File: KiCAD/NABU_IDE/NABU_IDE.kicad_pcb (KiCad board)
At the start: 2 copper layers, 80.8 x 69.5 mm, 18 parts, among them J1 IDE ATA Bus, J2 NABU Expansion Header, U1 74LS245, U2 74LS32, U3 74LS08, U4 74LS04, U5 74LS32, U6 74LS574, U7 74LS574

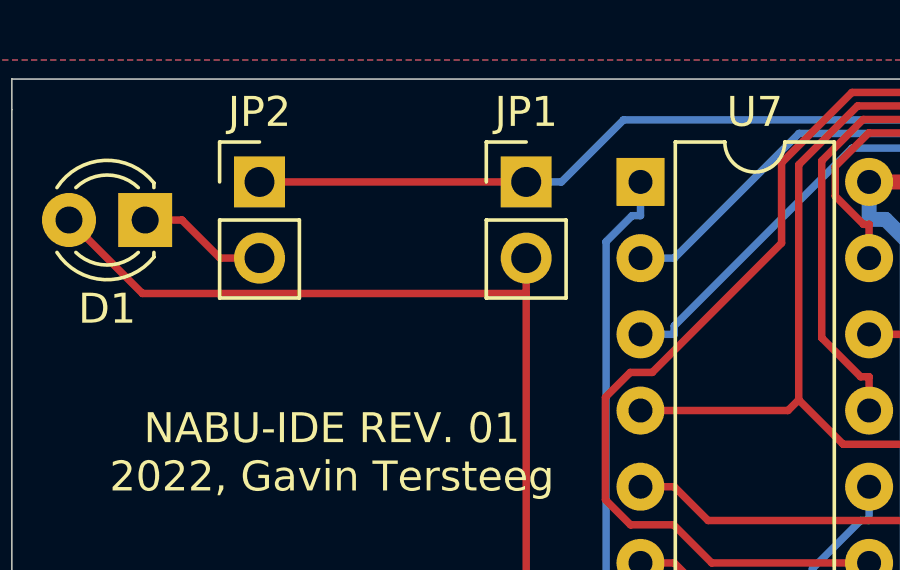
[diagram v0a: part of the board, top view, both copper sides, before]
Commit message: Changed schematics to allow for daisy chaining
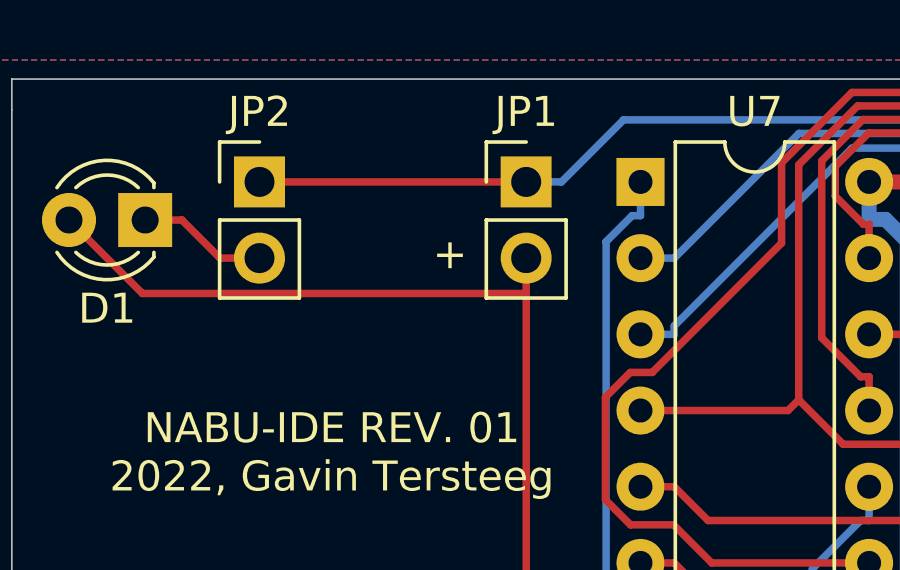
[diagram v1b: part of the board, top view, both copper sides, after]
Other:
- board text added: "+"
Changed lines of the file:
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@@
   (general
     (thickness 1.6)
-    (drawings 8)
+    (drawings 9)
     (tracks 862)
     (zones 0)
@@
     )
   )
+  (gr_text "+\n" (at 193.04 81.788) (layer F.SilkS)
+    (effects (font (size 1 1) (thickness 0.15)))
+  )
   (gr_line (start 259.207 141.097) (end 259.207 145.415) (layer Edge.Cuts) (width 0.05))

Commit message: Started work on new PCB layout
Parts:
- added C2: 100nf, Capacitor_THT:C_Rect_L7.2mm_W2.5mm_P5.00mm_FKS2_FKP2_MKS2_MKP2, F.Cu at (126.9, 54.1)
- added C3: 100nf, Capacitor_THT:C_Rect_L7.2mm_W2.5mm_P5.00mm_FKS2_FKP2_MKS2_MKP2, F.Cu at (116.0, 70.2)
- added C4: 100nf, Capacitor_THT:C_Rect_L7.2mm_W2.5mm_P5.00mm_FKS2_FKP2_MKS2_MKP2, F.Cu at (94.3, 77.0)
- added C5: 100nf, Capacitor_THT:C_Rect_L7.2mm_W2.5mm_P5.00mm_FKS2_FKP2_MKS2_MKP2, F.Cu at (94.3, 81.1)
- added C6: 100nf, Capacitor_THT:C_Rect_L7.2mm_W2.5mm_P5.00mm_FKS2_FKP2_MKS2_MKP2, F.Cu at (94.3, 85.1)
- added C7: 100nf, Capacitor_THT:C_Rect_L7.2mm_W2.5mm_P5.00mm_FKS2_FKP2_MKS2_MKP2, F.Cu at (83.5, 100.5)
- added C8: 100nf, Capacitor_THT:C_Rect_L7.2mm_W2.5mm_P5.00mm_FKS2_FKP2_MKS2_MKP2, F.Cu at (94.3, 89.2)
- added J3: NABU Daisy Chain In, Connector_PinHeader_2.54mm:PinHeader_1x30_P2.54mm_Vertical, F.Cu at (37.8, 50.3)
- added J4: NABU Daisy Chain Out, Connector_PinHeader_2.54mm:PinHeader_1x30_P2.54mm_Vertical, F.Cu at (33.2, 50.3)
- added J5: NABU External Power, Connector_Molex:Molex_KK-396_A-41791-0005_1x05_P3.96mm_Vertical, F.Cu at (106.2, 54.1)
- added R10: 10K, Resistor_THT:R_Axial_DIN0207_L6.3mm_D2.5mm_P10.16mm_Horizontal, F.Cu at (55.1, 114.6)
- added R11: 10K, Resistor_THT:R_Axial_DIN0207_L6.3mm_D2.5mm_P10.16mm_Horizontal, F.Cu at (55.1, 110.5)
- added R6: 10K, Resistor_THT:R_Axial_DIN0207_L6.3mm_D2.5mm_P10.16mm_Horizontal, F.Cu at (83.2, 96.4)
- added R7: 10K, Resistor_THT:R_Axial_DIN0207_L6.3mm_D2.5mm_P10.16mm_Horizontal, F.Cu at (55.1, 122.7)
- added R8: 10K, Resistor_THT:R_Axial_DIN0207_L6.3mm_D2.5mm_P10.16mm_Horizontal, F.Cu at (115.7, 62.1)
- added R9: 10K, Resistor_THT:R_Axial_DIN0207_L6.3mm_D2.5mm_P10.16mm_Horizontal, F.Cu at (68.4, 115.8)
- R1: value 50Ω -> 50R
- R2: value 180Ω -> 180R
- moved J2 225.4 mm to (51.2, 50.3), turned to 0 degrees
- moved J1 197.8 mm to (56.4, 54.1)
- moved R1 186.6 mm to (32.4, 128.3)
- moved R5 163.7 mm to (45.8, 128.3), turned to 0 degrees
- moved C1 162.6 mm to (59.4, 126.7)
- moved U5 153.1 mm to (72.4, 77.1)
- moved U1 147.6 mm to (94.1, 50.1)
- moved U4 145.3 mm to (104.9, 62.1)
- moved R4 143.1 mm to (55.1, 118.6)
- moved U6 139.6 mm to (83.2, 50.1)
- moved R2 138.6 mm to (115.7, 66.1), turned to 0 degrees
- moved U7 130.4 mm to (72.4, 50.1)
- moved R3 127.9 mm to (126.6, 50.0)
- moved U2 123.4 mm to (83.2, 77.1)
- moved U3 110.3 mm to (72.4, 96.5)
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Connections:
- U3 pad 12: GND -> Net-(R8-Pad1)
- U3 pad 13: GND -> Net-(R9-Pad1)
- U4 pad 13: GND -> Net-(R7-Pad1)
- U5 pad 12: GND -> Net-(R10-Pad1)
- U5 pad 13: GND -> Net-(R11-Pad1)
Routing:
- net GND: track 255.1 -> 0.00 mm
- net /+5V: track 190.9 -> 0.00 mm
- net /*IDE_ACTIVE: track 127.6 -> 0.00 mm
- net /*NABU_RD: track 106.9 -> 0.00 mm, vias 1 -> 0
- net /BUF_D4: track 103.4 -> 0.00 mm, vias 1 -> 0
- net /IDE_D10: track 100.8 -> 0.00 mm
- net /*IDE_CS0: track 100.2 -> 0.00 mm
- net /*NABU_RESET: track 97.0 -> 0.00 mm, vias 2 -> 0
- net /*IDE_WR: track 94.8 -> 0.00 mm, vias 1 -> 0
- net /NABU_A2: track 94.8 -> 0.00 mm
- net /NABU_A3: track 94.0 -> 0.00 mm
- net /BUF_D7: track 92.3 -> 0.00 mm, vias 1 -> 0
- net /NABU_D0: track 90.3 -> 0.00 mm
- net /BUF_D2: track 89.6 -> 0.00 mm, vias 1 -> 0
- net Net-(U5-Pad8): track 81.2 -> 0.00 mm, vias 1 -> 0
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- removed copper zone on B.Cu, net GND
- removed copper zone on F.Cu, net GND
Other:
- board outline removed
- board text removed: "+"
- board text removed: "NABU-IDE REV. 01 2022, Gavin Tersteeg"

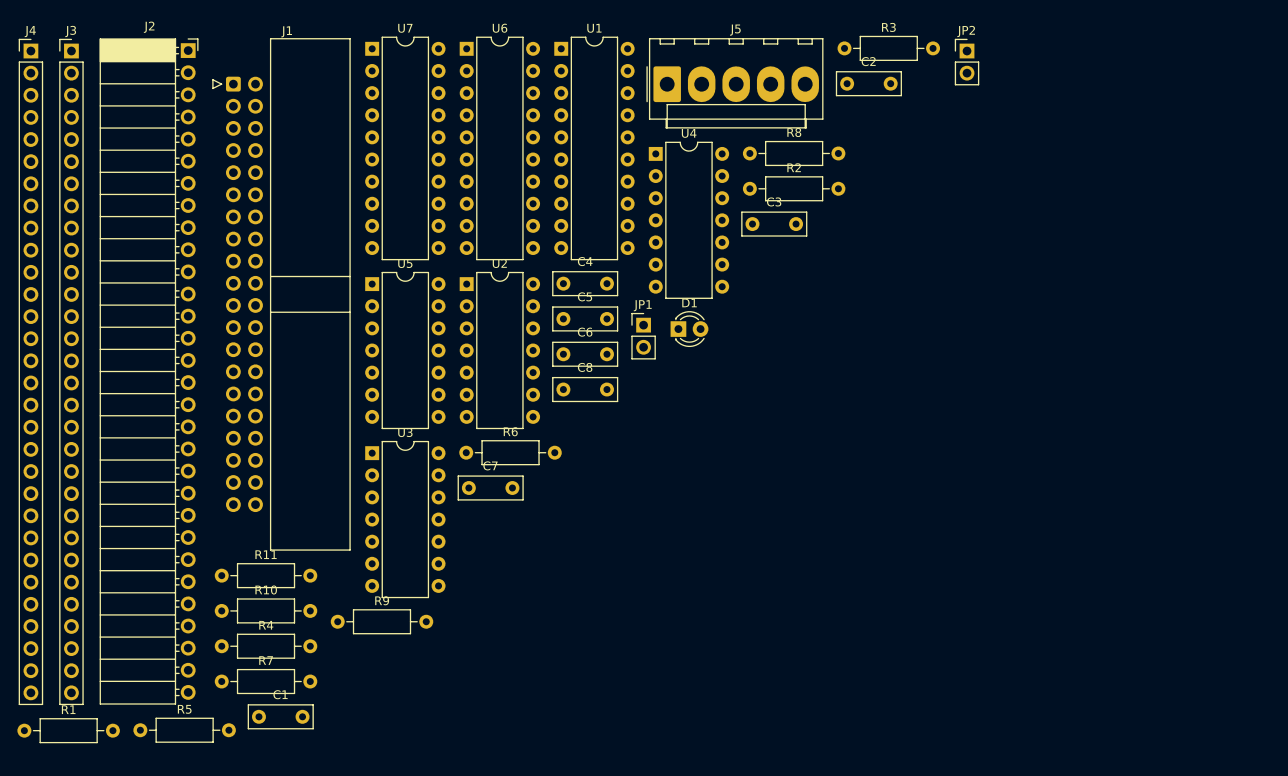
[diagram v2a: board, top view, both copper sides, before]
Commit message: Finished up most of the initial layout
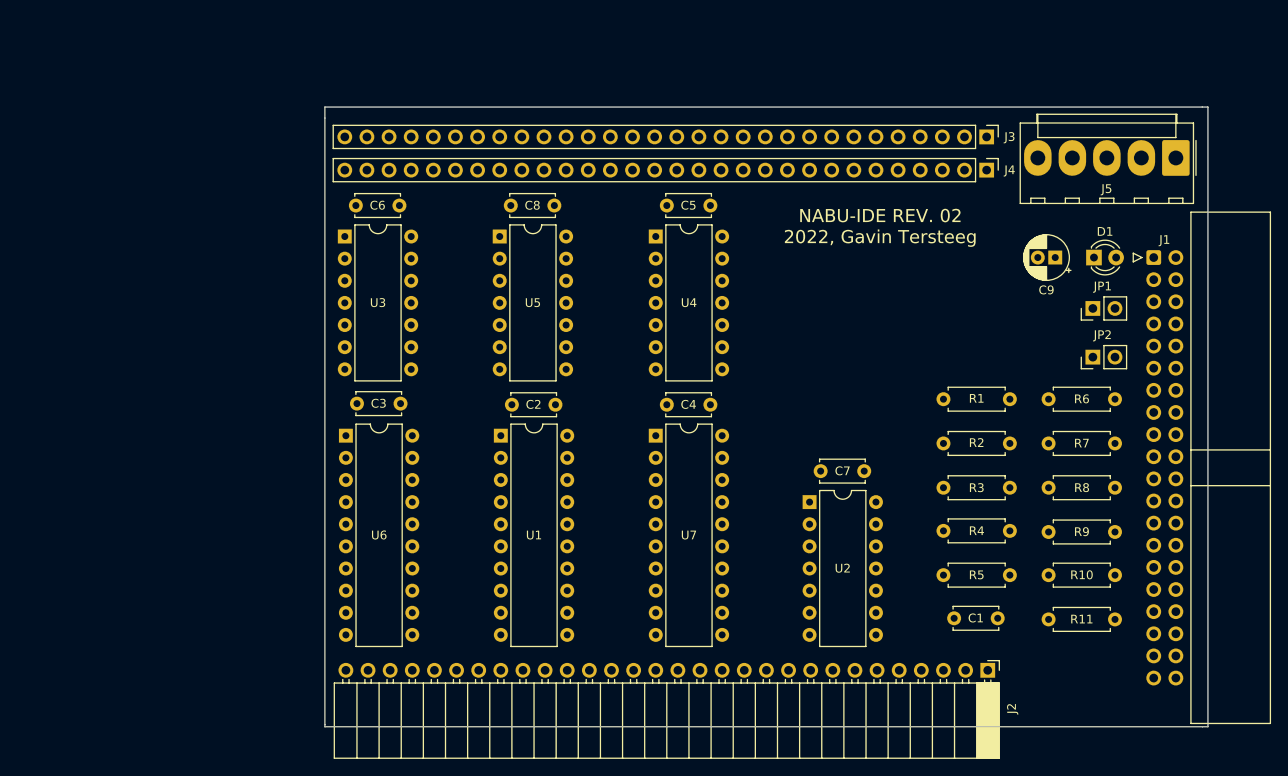
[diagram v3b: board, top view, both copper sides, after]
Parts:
- added C9: 100uf, Capacitor_THT:CP_Radial_D5.0mm_P2.00mm, F.Cu at (150.7, 74.0)
- C1, C2, C3, C4, C5, C6, C7, C8: footprint Capacitor_THT:C_Rect_L7.2mm_W2.5mm_P5.00mm_FKS2_FKP2_MKS2_MKP2 -> Capacitor_THT:C_Disc_D5.0mm_W2.5mm_P5.00mm
- R1, R10, R11, R2, R3, R4, R5, R6, R7, R8, R9: footprint Resistor_THT:R_Axial_DIN0207_L6.3mm_D2.5mm_P10.16mm_Horizontal -> Resistor_THT:R_Axial_DIN0207_L6.3mm_D2.5mm_P7.62mm_Horizontal
- moved J2 119.3 mm to (143.0, 126.5), turned to 270 degrees
- moved R1 112.1 mm to (137.9, 90.3)
- moved J4 110.5 mm to (142.9, 64.0), turned to 270 degrees
- moved J1 107.5 mm to (162.1, 74.0)
- moved R7 106.1 mm to (157.6, 95.4), turned to 180 degrees
- moved J3 105.5 mm to (142.9, 60.2), turned to 270 degrees
- moved R11 102.6 mm to (157.6, 115.6), turned to 180 degrees
- moved R10 102.6 mm to (157.6, 110.5), turned to 180 degrees
- moved R5 101.4 mm to (145.5, 110.5), turned to 180 degrees
- moved R4 91.4 mm to (145.5, 105.4), turned to 180 degrees
- moved R9 89.8 mm to (157.6, 105.5), turned to 180 degrees
- moved C1 80.6 mm to (139.1, 115.4)
- moved R6 67.1 mm to (150.0, 90.3)
- moved J5 59.0 mm to (164.6, 62.6), turned to 180 degrees
- moved R8 56.8 mm to (157.6, 100.5), turned to 180 degrees
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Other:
- board outline added: 101.3 x 71.1 mm
- board text added: "NABU-IDE REV. 02 2022, Gavin Tersteeg"

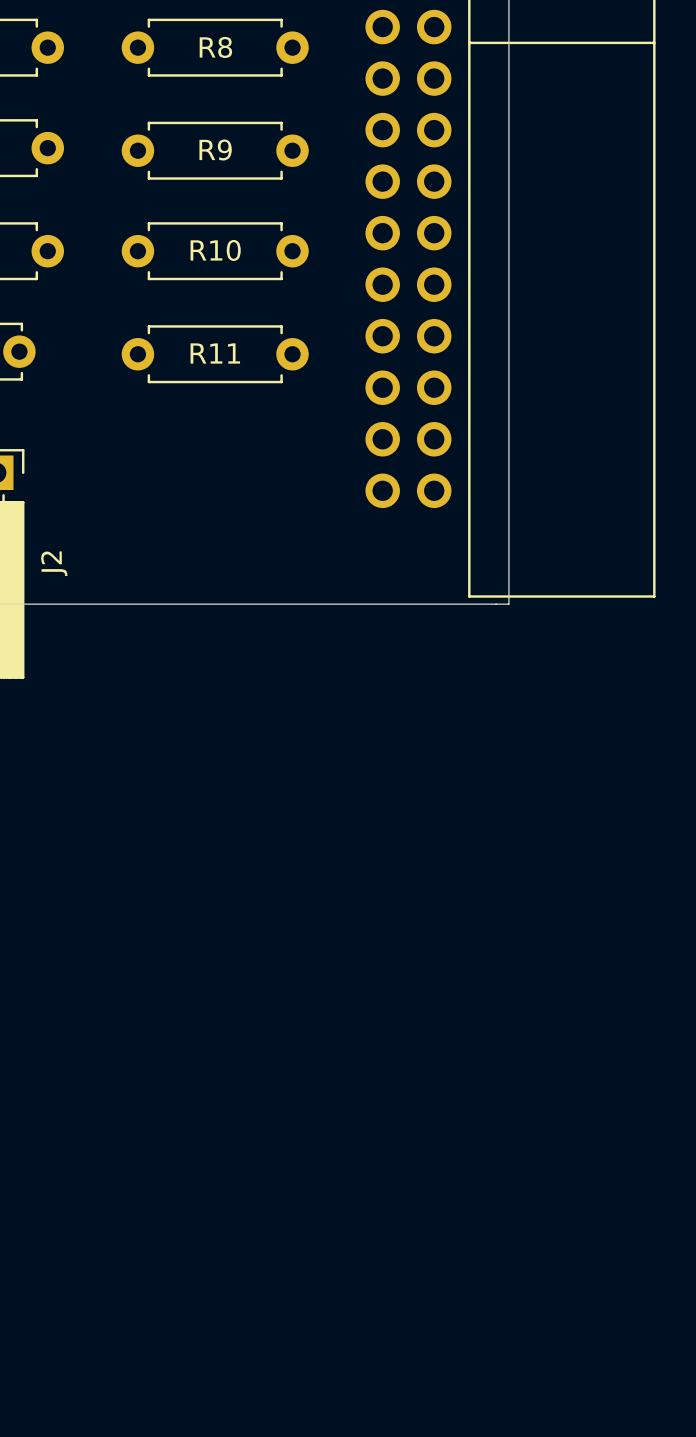
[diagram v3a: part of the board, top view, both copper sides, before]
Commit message: Updated PCB, but have not placed components yet
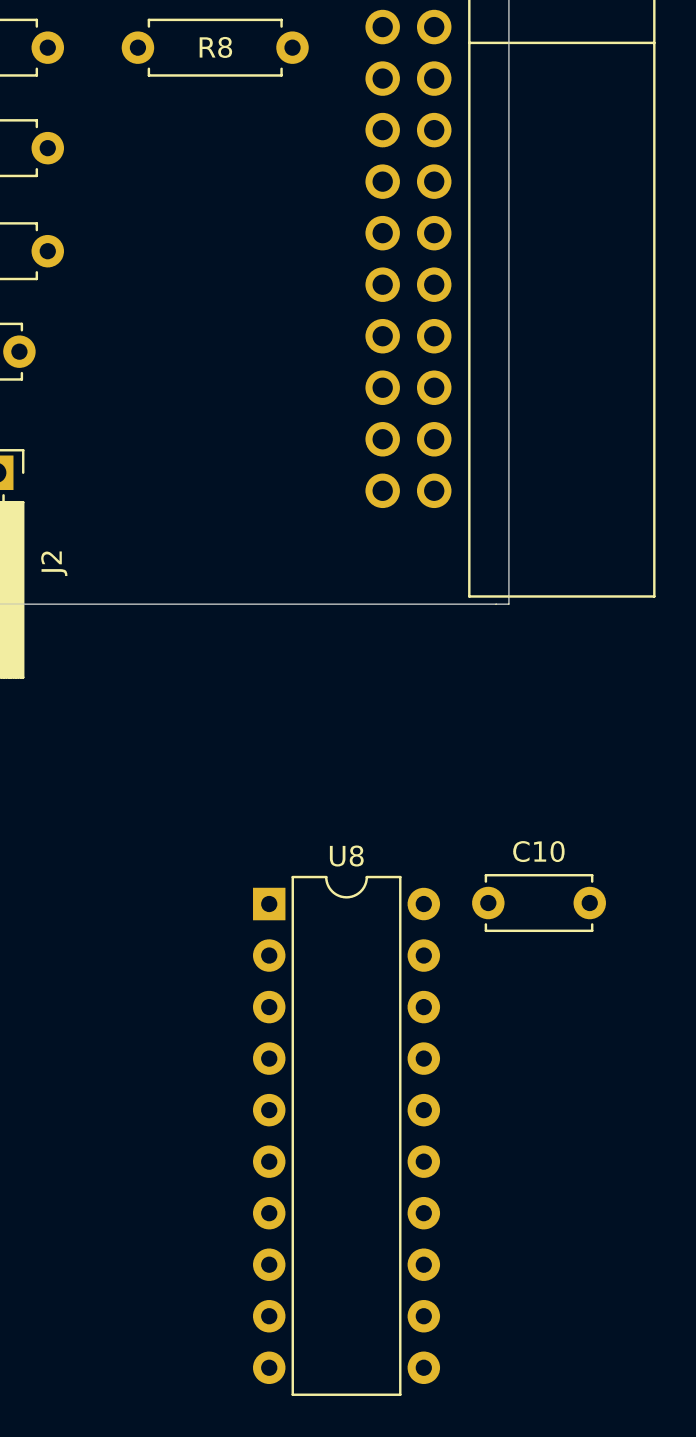
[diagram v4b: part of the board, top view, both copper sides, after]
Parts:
- removed R10, R11, R9: 10K, Resistor_THT:R_Axial_DIN0207_L6.3mm_D2.5mm_P7.62mm_Horizontal
- added C10: 100nf, Capacitor_THT:C_Disc_D5.0mm_W2.5mm_P5.00mm, F.Cu at (167.3, 142.6)
- added U8: 74LS245, Package_DIP:DIP-20_W7.62mm, F.Cu at (156.5, 142.7)
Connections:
- J1 pad 20: Net-(J1-Pad20) -> (no net)
- J1 pad 23: /*IDE_WR -> /*IDE_WR_BUF
- J1 pad 25: /*IDE_RD -> /*IDE_RD_BUF
- J1 pad 29: Net-(J1-Pad29) -> (no net)
- J1 pad 32: Net-(J1-Pad32) -> (no net)
- J1 pad 33: /NABU_A2 -> /NABU_A2_BUF
- J1 pad 34: Net-(J1-Pad34) -> (no net)
- J1 pad 35: /NABU_A1 -> /NABU_A1_BUF
- J1 pad 36: /NABU_A3 -> /NABU_A3_BUF
- J1 pad 37: /*IDE_CS0 -> /*IDE_CS0_BUF
- J1 pad 38: /*IDE_CS1 -> /*IDE_CS1_BUF
- J2 pad 10: Net-(J2-Pad10) -> (no net)
- J2 pad 14: Net-(J2-Pad14) -> (no net)
- J2 pad 2: Net-(J2-Pad2) -> (no net)
- J2 pad 29: Net-(J2-Pad29) -> (no net)
- J2 pad 3: Net-(J2-Pad3) -> (no net)
- J2 pad 30: Net-(J2-Pad30) -> (no net)
- J2 pad 4: Net-(J2-Pad4) -> (no net)
- J3 pad 1: Net-(J3-Pad1) -> (no net)
- J3 pad 10: Net-(J3-Pad10) -> (no net)
- J3 pad 4: Net-(J3-Pad4) -> (no net)
- J4 pad 1: Net-(J4-Pad1) -> (no net)
- J4 pad 10: Net-(J4-Pad10) -> (no net)
- J4 pad 26: Net-(J4-Pad26) -> (no net)
- J4 pad 30: Net-(J4-Pad30) -> (no net)
- J4 pad 4: Net-(J4-Pad4) -> (no net)
- J5 pad 3: Net-(J5-Pad3) -> (no net)
- U1 pad 19: Net-(U1-Pad19) -> /*NABU_SEL_DLY
- U2 pad 3: Net-(U1-Pad19) -> /*NABU_SEL
- U2 pad 4: Net-(U1-Pad19) -> /*NABU_SEL
- U3 pad 11: Net-(U3-Pad11) -> /*NABU_SEL_DLY
- U3 pad 12: Net-(R8-Pad1) -> Net-(U3-Pad12)
- U3 pad 13: Net-(R9-Pad1) -> Net-(R8-Pad1)
- U4 pad 12: Net-(U4-Pad12) -> (no net)
- U5 pad 12: Net-(R10-Pad1) -> GND
- U5 pad 13: Net-(R11-Pad1) -> /*IDE_WR_BUF
- U5 pad 2: Net-(U1-Pad19) -> /*NABU_SEL
- U6 pad 1: /*IDE_WR -> Net-(U5-Pad11)
